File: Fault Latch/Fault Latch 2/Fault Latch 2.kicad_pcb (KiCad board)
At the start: 2 copper layers, 105 x 100 mm, 80 parts, among them K101 Fujitsu_FTR-LYAA005x, K102 Fujitsu_FTR-LYAA005x, K103 Fujitsu_FTR-LYAA005x, Q104 Q_NPN_BEC, Q106 Q_NPN_BEC, Q107 Q_NPN_BEC, Q108 Q_NPN_BEC, Q109 Q_NMOS_GDS, Q110 Q_NMOS_GDS, Q111 Q_NMOS_GDS, Q112 Q_NPN_BEC, Q113 Q_NPN_BEC, SW101 SW_Omron_B3FS, SW102 SW_Omron_B3FS, SW103 SW_Omron_B3FS, U101 641964-1, U102 74AHC1G00, U103 74AHC1G00, U104 74AHC1G00, U105 641964-1, U106 74LS279, U107 SFH617A-1, U108 SFH617A-1, U109 SFH617A-1, U110 641964-1, U111 641964-1, U112 641964-1, U113 641964-1, U114 SFH617A-1, U115 SFH617A-1, U116 SFH617A-1

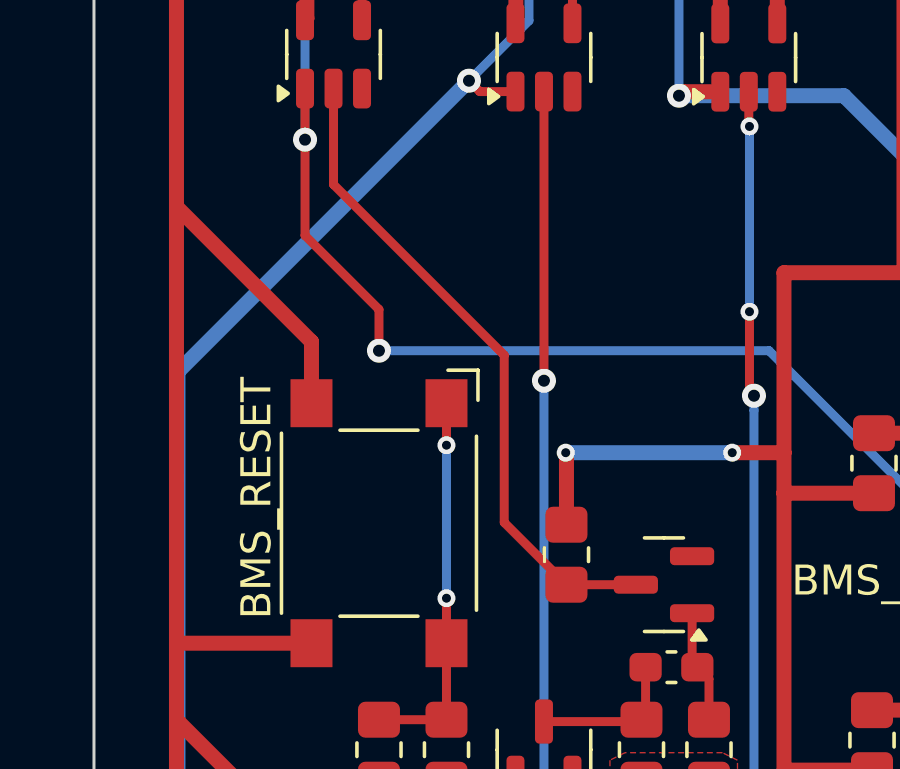
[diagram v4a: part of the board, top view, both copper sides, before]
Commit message: minor updates to fault latch and RML pcb layout
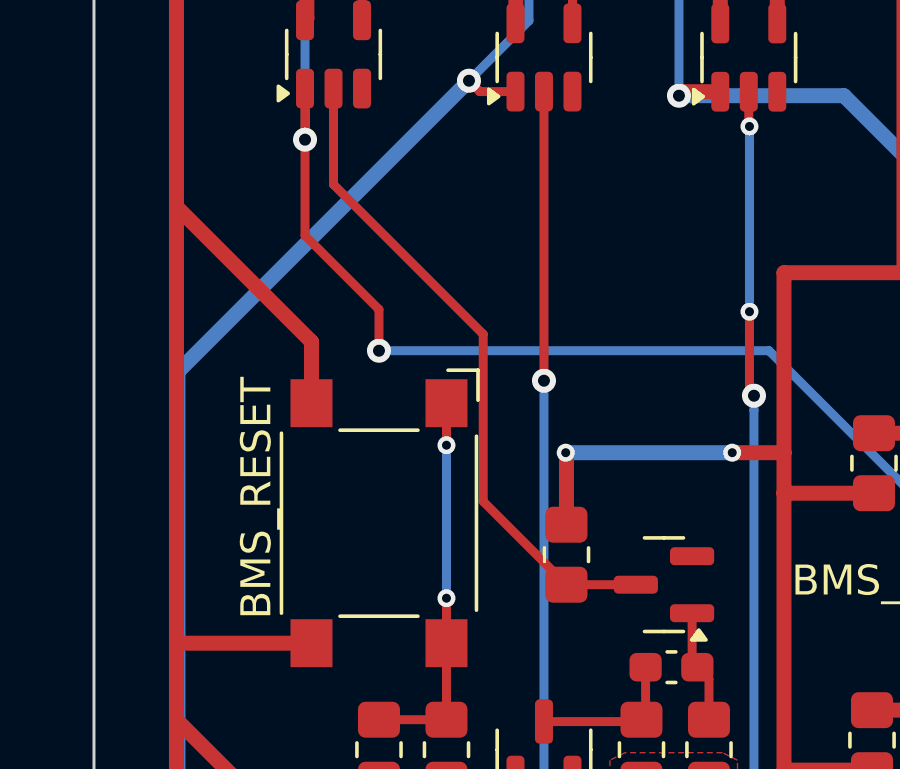
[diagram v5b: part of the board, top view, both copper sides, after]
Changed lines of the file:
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@@
 			(plot_on_all_layers_selection 0x00000000_00000000_00000000_00000000)
 			(disableapertmacros no)
-			(usegerberextensions no)
-			(usegerberattributes yes)
-			(usegerberadvancedattributes yes)
-			(creategerberjobfile yes)
+			(usegerberextensions yes)
+			(usegerberattributes no)
+			(usegerberadvancedattributes no)
+			(creategerberjobfile no)
 			(dashed_line_dash_ratio 12.000000)
 			(dashed_line_gap_ratio 3.000000)
@@
 			(sketchdnponfab yes)
 			(crossoutdnponfab yes)
-			(subtractmaskfromsilk no)
+			(subtractmaskfromsilk yes)
 			(outputformat 1)
 			(mirror no)
-			(drillshape 1)
+			(drillshape 0)
 			(scaleselection 1)
-			(outputdirectory "")
+			(outputdirectory "Gerber/")
 		)
 	)
@@
 	)
 	(segment
-		(start 88.675 96.725)
-		(end 90.75 98.8)
+		(start 87.975 90.45)
+		(end 87.975 96.025)
 		(width 0.3)
 		(layer "F.Cu")
@@
 	)
 	(segment
-		(start 90.75 98.8)
-		(end 93.0625 98.8)
+		(start 82.985 85.46)
+		(end 87.975 90.45)
 		(width 0.3)
 		(layer "F.Cu")
@@
 	)
 	(segment
-		(start 82.985 85.46)
-		(end 88.675 91.15)
+		(start 87.975 96.025)
+		(end 90.75 98.8)
 		(width 0.3)
 		(layer "F.Cu")
@@
 	)
 	(segment
-		(start 88.675 91.15)
-		(end 88.675 96.725)
+		(start 90.75 98.8)
+		(end 93.0625 98.8)
 		(width 0.3)
 		(layer "F.Cu")

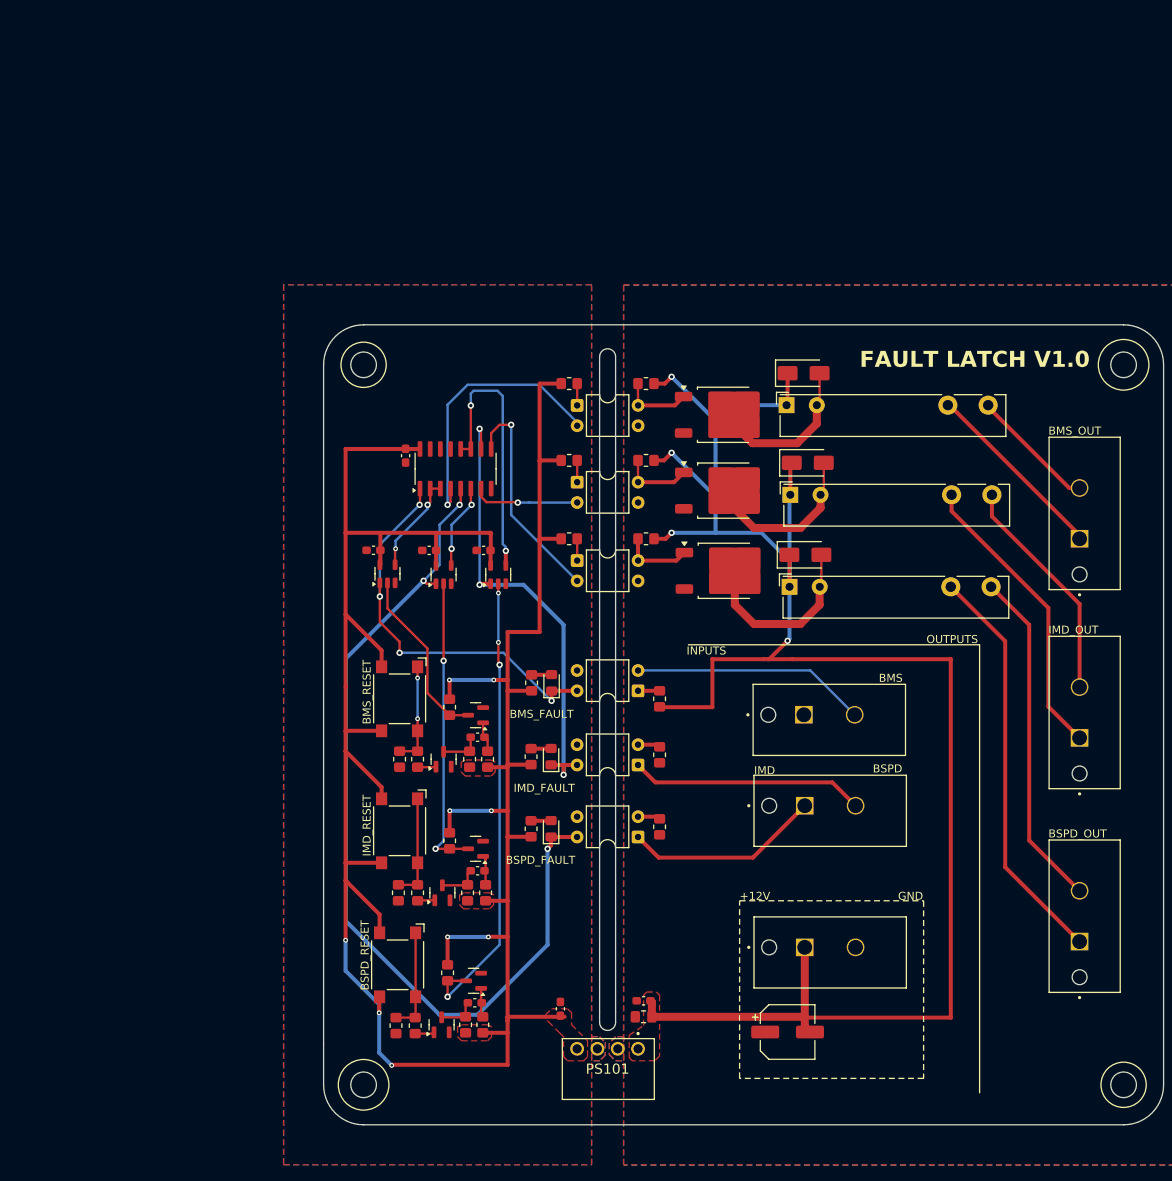
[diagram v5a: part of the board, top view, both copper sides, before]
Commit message: TSSI has been integrated into fault latch.
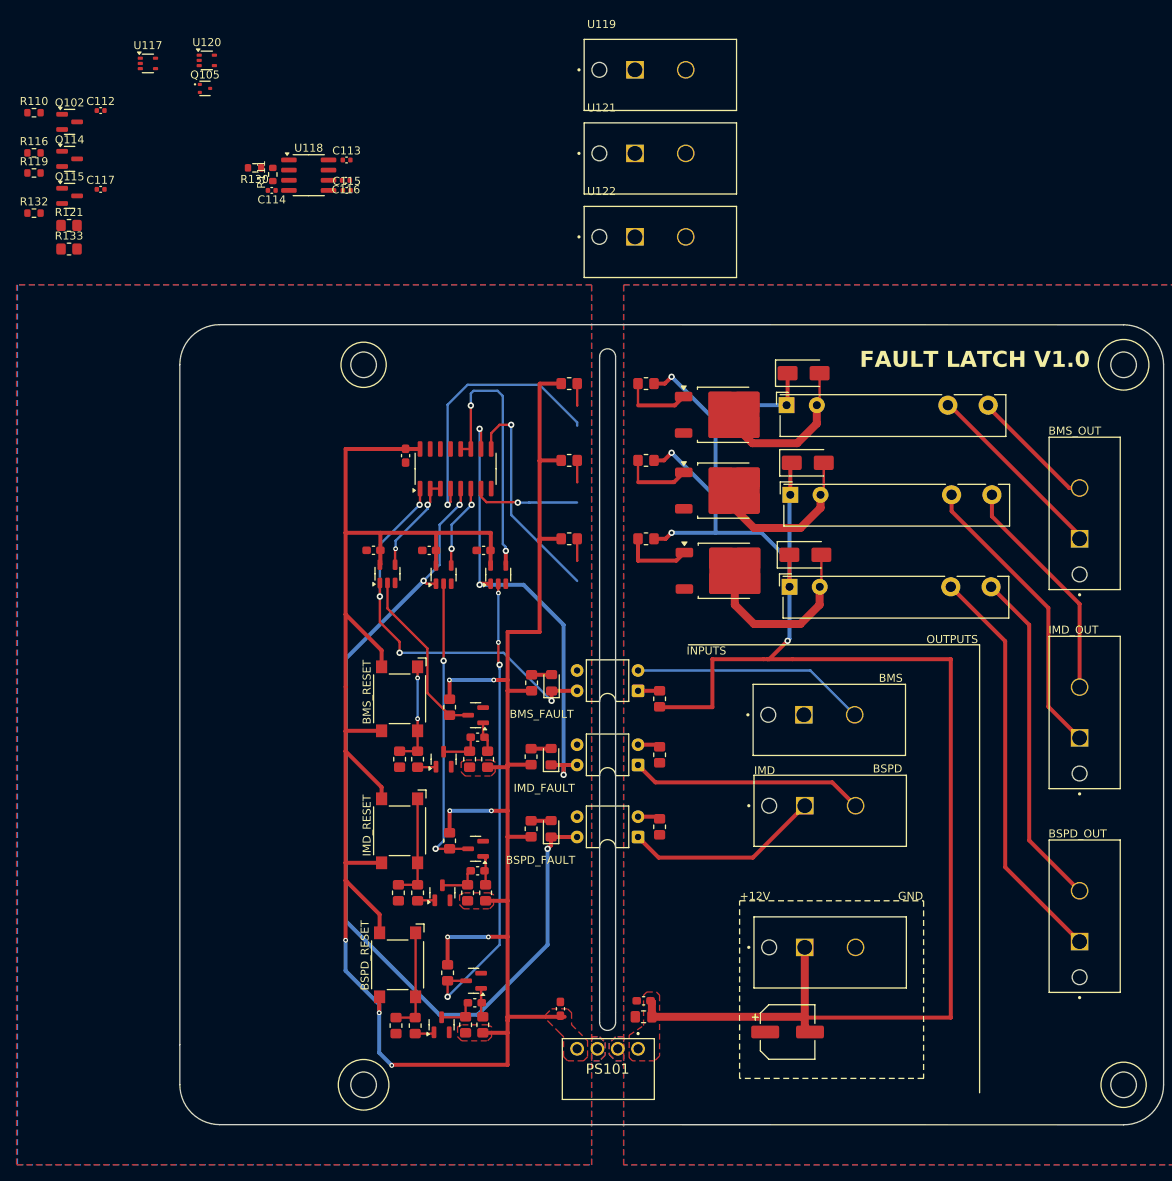
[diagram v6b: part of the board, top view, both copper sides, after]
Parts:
- removed U107, U108, U109: SFH617A-1, Package_DIP:DIP-4_W7.62mm
- added C112: 0.1u, Capacitor_SMD:C_0402_1005Metric, F.Cu at (47.1, 23.2)
- added C113: 1u, Capacitor_SMD:C_0402_1005Metric, F.Cu at (77.9, 29.4)
- added C114: 0.1u, Capacitor_SMD:C_0402_1005Metric, F.Cu at (68.5, 33.2)
- added C115: .01u, Capacitor_SMD:C_0402_1005Metric, F.Cu at (77.9, 33.2)
- added C116: 22u, Capacitor_SMD:C_0402_1005Metric, F.Cu at (77.8, 31.9)
- added C117: 0.1u, Capacitor_SMD:C_0402_1005Metric, F.Cu at (47.1, 33.1)
- added Q102: Q_NMOS_GSD, Package_TO_SOT_SMD:SOT-23, F.Cu at (43.2, 24.6)
- added Q105: Q_PMOS_GSD, Package_TO_SOT_SMD:SOT-523, F.Cu at (60.2, 20.4)
- added Q114: Q_NMOS_GSD, Package_TO_SOT_SMD:SOT-23, F.Cu at (43.2, 29.3)
- added Q115: Q_NMOS_GSD, Package_TO_SOT_SMD:SOT-23, F.Cu at (43.2, 33.9)
- added R110: 1k, Resistor_SMD:R_0603_1608Metric, F.Cu at (38.8, 23.5)
- added R111: 15k, Resistor_SMD:R_0603_1608Metric, F.Cu at (68.7, 31.2)
- added R116: 500R, Resistor_SMD:R_0603_1608Metric, F.Cu at (38.8, 28.5)
- added R119: 10k, Resistor_SMD:R_0603_1608Metric, F.Cu at (38.8, 31.0)
- added R121: 270R, Resistor_SMD:R_0805_2012Metric_Pad1.20x1.40mm_HandSolder, F.Cu at (43.2, 37.6)
- added R130: 100k, Resistor_SMD:R_0603_1608Metric, F.Cu at (66.4, 30.4)
- added R132: 1k, Resistor_SMD:R_0603_1608Metric, F.Cu at (38.8, 36.0)
- added R133: 270R, Resistor_SMD:R_0805_2012Metric_Pad1.20x1.40mm_HandSolder, F.Cu at (43.2, 40.5)
- added U117: 74AHC1G32, Package_TO_SOT_SMD:SOT-353_SC-70-5, F.Cu at (53.0, 17.3)
- added U118: LM555xM, Package_SO:SOIC-8_3.9x4.9mm_P1.27mm, F.Cu at (73.1, 31.3)
- added U119: 641964-1, 641964-1:TE_641964-1, F.Cu at (113.9, 18.1)
- added U120: 74AHC1G08, Package_TO_SOT_SMD:SOT-353_SC-70-5, F.Cu at (60.4, 16.9)
- added U121: 641964-1, 641964-1:TE_641964-1, F.Cu at (113.9, 28.6)
- added U122: 641964-1, 641964-1:TE_641964-1, F.Cu at (113.9, 39.0)
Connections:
- D104 pad 1: +12V -> +5V
- D105 pad 1: +12V -> +5V
- D106 pad 1: +12V -> +5V
- K101 pad A1: +12V -> +5V
- K102 pad A1: +12V -> +5V
- K103 pad A1: +12V -> +5V
- R118 pad 1: Net-(R118-Pad1) -> Net-(Q111-G)
- U106 pad 4: Net-(U106A-Q) -> Net-(Q109-G)
- U106 pad 7: Net-(U106B-Q) -> Net-(Q110-G)
- U106 pad 9: Net-(U106C-Q) -> Net-(Q111-G)
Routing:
- net Net-(U106A-Q): track 34.3 -> 0.00 mm, vias 1 -> 0
- net Net-(Q109-G): track 8.87 -> 43.1 mm, vias 0 -> 1
- net Net-(Q111-G): track 8.93 -> 39.5 mm, vias 0 -> 1
- net Net-(U106C-Q): track 27.8 -> 0.00 mm, vias 1 -> 0
- net Net-(U106B-Q): track 13.3 -> 0.00 mm, vias 1 -> 0
- net Net-(Q110-G): track 8.95 -> 22.3 mm, vias 0 -> 1
- net Net-(R118-Pad1): track 2.73 -> 0.00 mm
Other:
- board size 105 x 100 mm -> 123 x 100 mm
